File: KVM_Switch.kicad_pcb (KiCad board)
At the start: 2 copper layers, 6 parts, among them J1 HDMI_A, J2 HDMI_A, U1 USB2514B_Bi, U2 STM32C011F4Px, U3 TS3USB221AQRSERQ1, U4 HD3SS215RTQR

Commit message: Moved stuff armound & added components
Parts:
- added J3: USB_C_Receptacle_USB2.0_16P, Connector_USB:USB_C_Receptacle_GCT_USB4105-xx-A_16P_TopMnt_Horizontal, F.Cu at (188.8, 110.6)
- added J4: USB_C_Receptacle_USB2.0_16P, Connector_USB:USB_C_Receptacle_GCT_USB4105-xx-A_16P_TopMnt_Horizontal, F.Cu at (188.8, 120.6)
- added J5: USB_C_Receptacle_USB2.0_16P, Connector_USB:USB_C_Receptacle_GCT_USB4105-xx-A_16P_TopMnt_Horizontal, F.Cu at (188.8, 130.6)
- added U5: TPD12S016PWR, Package_SO:TSSOP-24_4.4x7.8mm_P0.65mm, F.Cu at (113.0, 91.3)
- moved J2 33.9 mm to (158.9, 77.7)
- moved U3 3.86 mm to (153.1, 123.4)
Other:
- board outline added: 100 x 100 mm

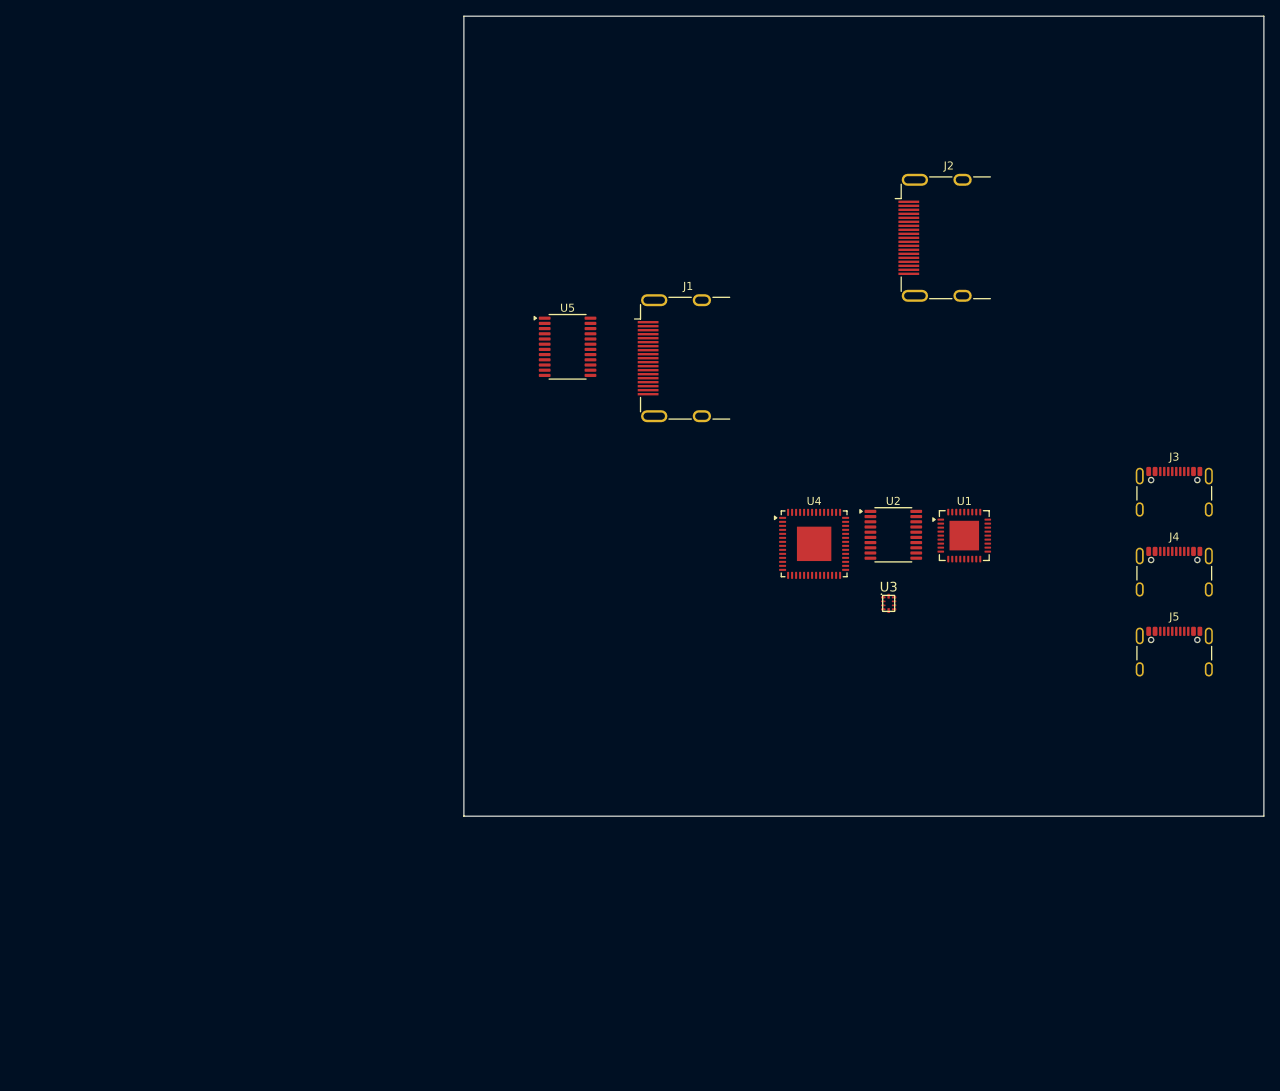
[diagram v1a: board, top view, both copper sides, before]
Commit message: Updated library structure
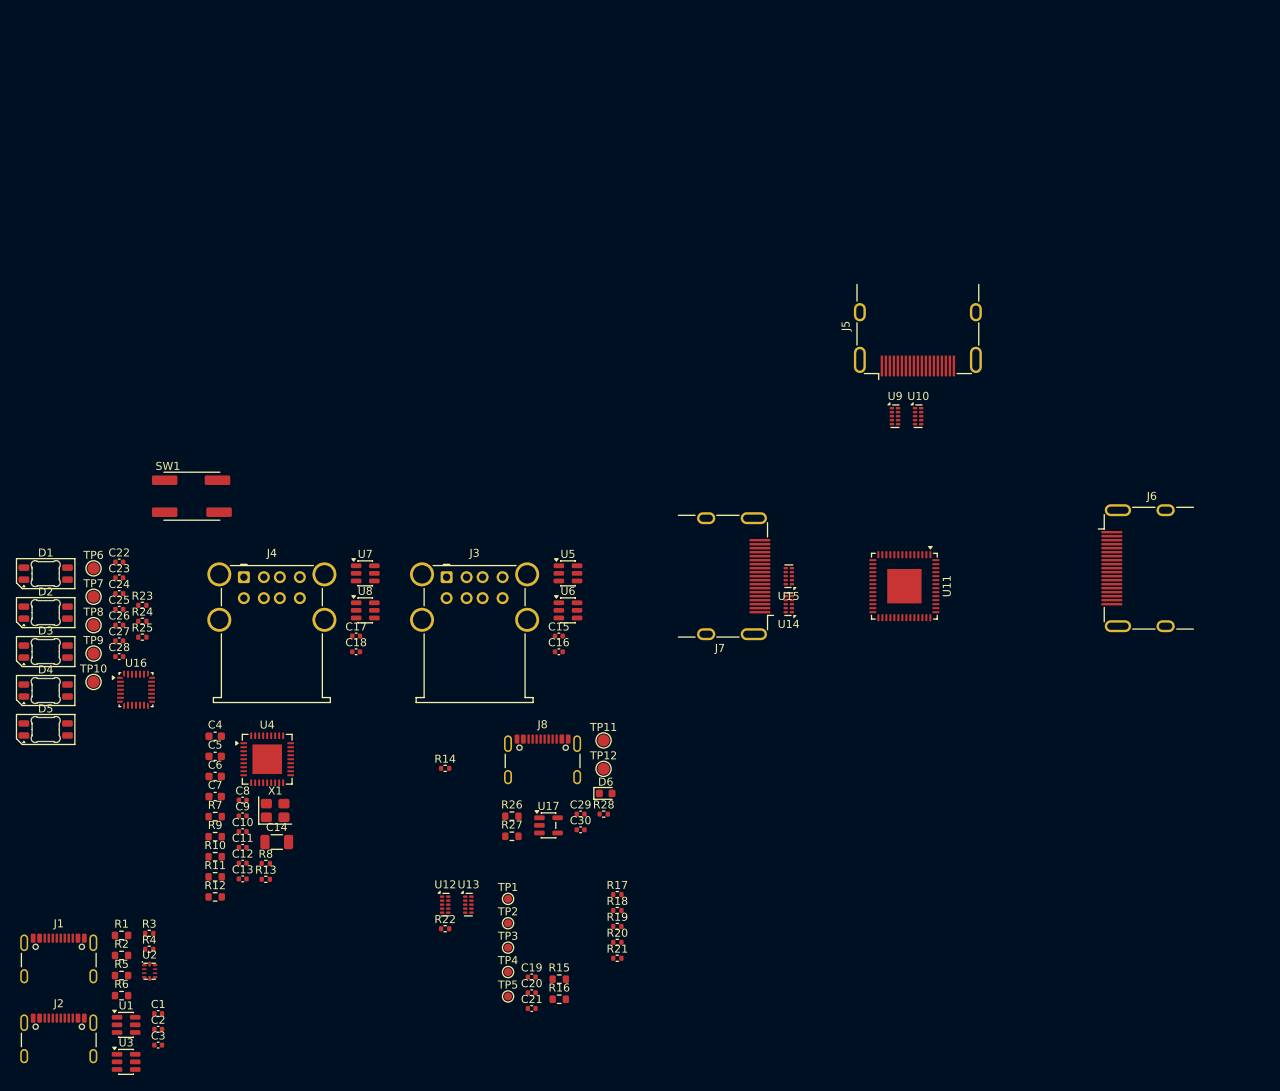
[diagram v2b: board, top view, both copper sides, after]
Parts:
- added C1: 1u, Capacitor_SMD:C_0402_1005Metric, F.Cu at (61.8, 174.7)
- added C10: 1u, Capacitor_SMD:C_0402_1005Metric, F.Cu at (72.3, 151.9)
- added C11: 1u, Capacitor_SMD:C_0402_1005Metric, F.Cu at (72.3, 153.9)
- added C12: 1u, Capacitor_SMD:C_0402_1005Metric, F.Cu at (72.3, 155.9)
- added C13: 1u, Capacitor_SMD:C_0402_1005Metric, F.Cu at (72.3, 157.8)
- added C14: 100u, Capacitor_SMD:C_1206_3216Metric, F.Cu at (76.6, 153.2)
- added C15: 1u, Capacitor_SMD:C_0402_1005Metric, F.Cu at (111.9, 127.5)
- added C16: 1u, Capacitor_SMD:C_0402_1005Metric, F.Cu at (111.9, 129.4)
- added C17: 1u, Capacitor_SMD:C_0402_1005Metric, F.Cu at (86.5, 127.5)
- added C18: 1u, Capacitor_SMD:C_0402_1005Metric, F.Cu at (86.5, 129.4)
- added C19: 1u, Capacitor_SMD:C_0402_1005Metric, F.Cu at (108.5, 170.1)
- added C2: 1u, Capacitor_SMD:C_0402_1005Metric, F.Cu at (61.8, 176.6)
- added C20: 1u, Capacitor_SMD:C_0402_1005Metric, F.Cu at (108.5, 172.1)
- added C21: 1u, Capacitor_SMD:C_0402_1005Metric, F.Cu at (108.5, 174.0)
- added C22: 1u, Capacitor_SMD:C_0402_1005Metric, F.Cu at (56.9, 118.2)
- added C23: 1u, Capacitor_SMD:C_0402_1005Metric, F.Cu at (56.9, 120.2)
- added C24: 1u, Capacitor_SMD:C_0402_1005Metric, F.Cu at (56.9, 122.2)
- added C25: 1u, Capacitor_SMD:C_0402_1005Metric, F.Cu at (56.9, 124.1)
- added C26: 1u, Capacitor_SMD:C_0402_1005Metric, F.Cu at (56.9, 126.1)
- added C27: 1u, Capacitor_SMD:C_0402_1005Metric, F.Cu at (56.9, 128.1)
- added C28: 1u, Capacitor_SMD:C_0402_1005Metric, F.Cu at (56.9, 130.1)
- added C29: 1u, Capacitor_SMD:C_0402_1005Metric, F.Cu at (114.6, 149.7)
- added C3: 1u, Capacitor_SMD:C_0402_1005Metric, F.Cu at (61.8, 178.6)
- added C30: 1u, Capacitor_SMD:C_0402_1005Metric, F.Cu at (114.6, 151.7)
- added C4: 10p, Capacitor_SMD:C_0603_1608Metric, F.Cu at (68.9, 140.0)
- added C5: 100n, Capacitor_SMD:C_0603_1608Metric, F.Cu at (68.9, 142.5)
- added C6: 10p, Capacitor_SMD:C_0603_1608Metric, F.Cu at (68.9, 145.0)
- added C7: 100n, Capacitor_SMD:C_0603_1608Metric, F.Cu at (68.9, 147.5)
- added C8: 1u, Capacitor_SMD:C_0402_1005Metric, F.Cu at (72.3, 148.0)
- added C9: 1u, Capacitor_SMD:C_0402_1005Metric, F.Cu at (72.3, 150.0)
- added D1: SK6812MINI-E, LED_SMD:LED_SK6812MINI-E_3.2x2.8mm_P1.5mm_ReverseMount, F.Cu at (47.7, 119.7)
- added D2: SK6812MINI-E, LED_SMD:LED_SK6812MINI-E_3.2x2.8mm_P1.5mm_ReverseMount, F.Cu at (47.7, 124.5)
- added D3: SK6812MINI-E, LED_SMD:LED_SK6812MINI-E_3.2x2.8mm_P1.5mm_ReverseMount, F.Cu at (47.7, 129.4)
- added D4: SK6812MINI-E, LED_SMD:LED_SK6812MINI-E_3.2x2.8mm_P1.5mm_ReverseMount, F.Cu at (47.7, 134.3)
- added D5: SK6812MINI-E, LED_SMD:LED_SK6812MINI-E_3.2x2.8mm_P1.5mm_ReverseMount, F.Cu at (47.7, 139.2)
- added D6: GLED, LED_SMD:LED_0603_1608Metric, F.Cu at (117.7, 147.2)
- added J6: HDMI_A, Connector_Video:HDMI_A_Molex_208658-1001_Horizontal, F.Cu at (184.3, 119.0)
- added J7: HDMI_A, Connector_Video:HDMI_A_Molex_208658-1001_Horizontal, F.Cu at (133.7, 120.0)
- added J8: USB_C_Receptacle_USB2.0_16P, Connector_USB:USB_C_Receptacle_GCT_USB4105-xx-A_16P_TopMnt_Horizontal, F.Cu at (109.8, 144.0)
- added R1: 5.1k, Resistor_SMD:R_0603_1608Metric, F.Cu at (57.2, 164.9)
- added R10: 100k, Resistor_SMD:R_0603_1608Metric, F.Cu at (68.9, 155.1)
- added R11: 100k, Resistor_SMD:R_0603_1608Metric, F.Cu at (68.9, 157.6)
- added R12: 100k, Resistor_SMD:R_0603_1608Metric, F.Cu at (68.9, 160.1)
- added R13: 10k, Resistor_SMD:R_0402_1005Metric, F.Cu at (75.2, 157.9)
- added R14: 10k, Resistor_SMD:R_0402_1005Metric, F.Cu at (97.7, 144.0)
- added R15: 100k, Resistor_SMD:R_0603_1608Metric, F.Cu at (111.9, 170.4)
- added R16: 100k, Resistor_SMD:R_0603_1608Metric, F.Cu at (111.9, 172.9)
- added R17: 47k, Resistor_SMD:R_0402_1005Metric, F.Cu at (119.2, 159.8)
- added R18: 10k, Resistor_SMD:R_0402_1005Metric, F.Cu at (119.2, 161.8)
- added R19: 47k, Resistor_SMD:R_0402_1005Metric, F.Cu at (119.2, 163.8)
- added R2: 5.1k, Resistor_SMD:R_0603_1608Metric, F.Cu at (57.2, 167.4)
- added R20: 10k, Resistor_SMD:R_0402_1005Metric, F.Cu at (119.2, 165.8)
- added R21: 10k, Resistor_SMD:R_0402_1005Metric, F.Cu at (119.2, 167.8)
- added R22: 10k, Resistor_SMD:R_0402_1005Metric, F.Cu at (97.7, 164.1)
- added R23: 10k, Resistor_SMD:R_0402_1005Metric, F.Cu at (59.8, 123.6)
- added R24: 10k, Resistor_SMD:R_0402_1005Metric, F.Cu at (59.8, 125.6)
- added R25: 10k, Resistor_SMD:R_0402_1005Metric, F.Cu at (59.8, 127.6)
- added R26: 5.1k, Resistor_SMD:R_0603_1608Metric, F.Cu at (106.0, 150.0)
- added R27: 5.1k, Resistor_SMD:R_0603_1608Metric, F.Cu at (106.0, 152.5)
- added R28: 470, Resistor_SMD:R_0402_1005Metric, F.Cu at (117.5, 149.7)
- added R3: 10k, Resistor_SMD:R_0402_1005Metric, F.Cu at (60.7, 164.6)
- added R4: 10k, Resistor_SMD:R_0402_1005Metric, F.Cu at (60.7, 166.6)
- added R5: 5.1k, Resistor_SMD:R_0603_1608Metric, F.Cu at (57.2, 169.9)
- added R6: 5.1k, Resistor_SMD:R_0603_1608Metric, F.Cu at (57.2, 172.4)
- added R7: 100k, Resistor_SMD:R_0603_1608Metric, F.Cu at (68.9, 150.1)
- added R8: 10k, Resistor_SMD:R_0402_1005Metric, F.Cu at (75.2, 155.9)
- added R9: 12k, Resistor_SMD:R_0603_1608Metric, F.Cu at (68.9, 152.6)
- added SW1: SPST-NO, KVM_Swtich:EVQ-Q2K03W, F.Cu at (66.0, 110.0)
- added TP1: TestPoint, TestPoint:TestPoint_Pad_D1.0mm, F.Cu at (105.5, 160.3)
- added TP10: TestPoint, TestPoint:TestPoint_Pad_D1.5mm, F.Cu at (53.7, 133.2)
- added TP11: TestPoint, TestPoint:TestPoint_Pad_D1.5mm, F.Cu at (117.5, 140.5)
- added TP12: TestPoint, TestPoint:TestPoint_Pad_D1.5mm, F.Cu at (117.5, 144.1)
- added TP2: TestPoint, TestPoint:TestPoint_Pad_D1.0mm, F.Cu at (105.5, 163.4)
- added TP3: TestPoint, TestPoint:TestPoint_Pad_D1.0mm, F.Cu at (105.5, 166.4)
- added TP4: TestPoint, TestPoint:TestPoint_Pad_D1.0mm, F.Cu at (105.5, 169.5)
- added TP5: TestPoint, TestPoint:TestPoint_Pad_D1.0mm, F.Cu at (105.5, 172.5)
- added TP6: TestPoint, TestPoint:TestPoint_Pad_D1.5mm, F.Cu at (53.7, 119.0)
- added TP7: TestPoint, TestPoint:TestPoint_Pad_D1.5mm, F.Cu at (53.7, 122.6)
- added TP8: TestPoint, TestPoint:TestPoint_Pad_D1.5mm, F.Cu at (53.7, 126.1)
- added TP9: TestPoint, TestPoint:TestPoint_Pad_D1.5mm, F.Cu at (53.7, 129.7)
- added U10: TPD4E02B04DQA, Package_SON:USON-10_2.5x1.0mm_P0.5mm, F.Cu at (156.8, 100.0)
- added U11: HD3SS215RTQR, Package_DFN_QFN:QFN-56-1EP_8x8mm_P0.5mm_EP4.3x4.3mm, F.Cu at (155.1, 121.2)
- added U12: TPD4E02B04DQA, Package_SON:USON-10_2.5x1.0mm_P0.5mm, F.Cu at (97.7, 161.1)
- added U13: TPD4E02B04DQA, Package_SON:USON-10_2.5x1.0mm_P0.5mm, F.Cu at (100.6, 161.1)
- added U14: TPD4E02B04DQA, Package_SON:USON-10_2.5x1.0mm_P0.5mm, F.Cu at (140.6, 123.5)
- added U15: TPD4E02B04DQA, Package_SON:USON-10_2.5x1.0mm_P0.5mm, F.Cu at (140.6, 120.0)
- added U16: STM32C031G6Ux, Package_DFN_QFN:QFN-28_4x4mm_P0.5mm, F.Cu at (59.0, 134.2)
- added U17: TLV75533PDBV, Package_TO_SOT_SMD:SOT-23-5, F.Cu at (110.6, 151.1)
- added U6: USBLC6-2SC6, Package_TO_SOT_SMD:SOT-23-6, F.Cu at (113.0, 124.3)
- added U7: USBLC6-2SC6, Package_TO_SOT_SMD:SOT-23-6, F.Cu at (87.7, 119.6)
- added U8: USBLC6-2SC6, Package_TO_SOT_SMD:SOT-23-6, F.Cu at (87.7, 124.3)
- added U9: TPD4E02B04DQA, Package_SON:USON-10_2.5x1.0mm_P0.5mm, F.Cu at (153.9, 100.0)
- added X1: 24MHz, Crystal:Crystal_SMD_3225-4Pin_3.2x2.5mm, F.Cu at (76.4, 149.3)
- J1, J2: value HDMI_A -> USB_C_Receptacle_USB2.0_16P; footprint Connector_Video:HDMI_A_Molex_208658-1001_Horizontal -> Connector_USB:USB_C_Receptacle_GCT_USB4105-xx-A_16P_TopMnt_Horizontal
- J3, J4: value USB_C_Receptacle_USB2.0_16P -> USB_A_Stacked; footprint Connector_USB:USB_C_Receptacle_GCT_USB4105-xx-A_16P_TopMnt_Horizontal -> Connector_USB:USB_A_Wuerth_61400826021_Horizontal_Stacked
- J5: value USB_C_Receptacle_USB2.0_16P -> HDMI_A; footprint Connector_USB:USB_C_Receptacle_GCT_USB4105-xx-A_16P_TopMnt_Horizontal -> Connector_Video:HDMI_A_Molex_208658-1001_Horizontal
- U1: value USB2514B_Bi -> USBLC6-2SC6; footprint Package_DFN_QFN:QFN-36-1EP_6x6mm_P0.5mm_EP3.7x3.7mm -> Package_TO_SOT_SMD:SOT-23-6
- U2: value STM32C011F4Px -> TS3USB221AQRSERQ1; footprint Package_SO:TSSOP-20_4.4x6.5mm_P0.65mm -> TS3USB221AQRSERQ1:TS3USB221AQRSERQ1
- U3: value TS3USB221AQRSERQ1 -> USBLC6-2SC6; footprint TS3USB221AQRSERQ1:TS3USB221AQRSERQ1 -> Package_TO_SOT_SMD:SOT-23-6
- U4: value HD3SS215RTQR -> USB2514B_Bi; footprint Package_DFN_QFN:QFN-56-1EP_8x8mm_P0.5mm_EP4.3x4.3mm -> Package_DFN_QFN:QFN-36-1EP_6x6mm_P0.5mm_EP3.7x3.7mm
- U5: value TPD12S016PWR -> USBLC6-2SC6; footprint Package_SO:TSSOP-24_4.4x7.8mm_P0.65mm -> Package_TO_SOT_SMD:SOT-23-6
- moved J2 149.1 mm to (49.4, 178.9)
- moved U1 121.3 mm to (57.8, 176.1)
- moved J4 116.3 mm to (72.5, 120.1)
- moved U3 111.2 mm to (57.8, 180.7)
- moved J1 108.3 mm to (49.4, 168.9)
- moved U2 107.8 mm to (60.7, 169.4)
- moved J3 91.5 mm to (97.8, 120.1)
- moved U4 73.5 mm to (75.4, 142.9)
- moved J5 51.4 mm to (156.8, 90.4), turned to 90 degrees
- moved U5 28.3 mm to (113.0, 119.6)
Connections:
- J1 pad SH: unconnected-(J1-PadSH) -> GND
- J2 pad SH: unconnected-(J2-PadSH) -> GND
- J3 pad SH: unconnected-(J3-SHIELD-PadSH) -> Net-(J3-GND2)
- J4 pad SH: unconnected-(J4-SHIELD-PadSH) -> Net-(J4-GND2)
- J5 pad SH: unconnected-(J5-SHIELD-PadSH) -> GND
- U1 pad 1: unconnected-(U1-USBDM_DN1/PRT_DIS_M1-Pad1) -> /USB_Host_Select/USB_CONN_A_DN
- U1 pad 2: unconnected-(U1-USBDP_DN1/PRT_DIS_P1-Pad2) -> GND
- U1 pad 3: unconnected-(U1-USBDM_DN2/PRT_DIS_M2-Pad3) -> /USB_Host_Select/USB_CONN_A_DP
- U1 pad 4: unconnected-(U1-USBDP_DN2/PRT_DIS_P2-Pad4) -> /USB_Host_Select/USB_A_DP
- U1 pad 5: unconnected-(U1-VDDA33-Pad5) -> Net-(U1-VBUS)
- U1 pad 6: unconnected-(U1-USBDM_DN3/PRT_DIS_M3-Pad6) -> /USB_Host_Select/USB_A_DN
- U2 pad 1: unconnected-(U2-PB7-Pad1) -> /USB_Host_Select/USB_A_DP
- U2 pad 10: unconnected-(U2-PA3-Pad10) -> +3V3
- U2 pad 2: unconnected-(U2-PC14-Pad2) -> /USB_Host_Select/USB_A_DN
- U2 pad 3: unconnected-(U2-PC15-Pad3) -> /USB_Host_Select/USB_B_DP
- U2 pad 4: unconnected-(U2-VDD-Pad4) -> /USB_Host_Select/USB_B_DN
- U2 pad 5: unconnected-(U2-VSS-Pad5) -> GND
- U2 pad 6: unconnected-(U2-PF2-Pad6) -> Net-(U2-~{OE})
- U2 pad 7: unconnected-(U2-PA0-Pad7) -> /UBS_Hub/USB_UP_DN
- U2 pad 8: unconnected-(U2-PA1-Pad8) -> /UBS_Hub/USB_UP_DP
- U2 pad 9: unconnected-(U2-PA2-Pad9) -> /SW
- U3 pad 1: unconnected-(U3-1D+-Pad1) -> /USB_Host_Select/USB_CONN_B_DN
- U3 pad 2: unconnected-(U3-1D--Pad2) -> GND
- U3 pad 3: unconnected-(U3-2D+-Pad3) -> /USB_Host_Select/USB_CONN_B_DP
- U3 pad 4: unconnected-(U3-2D--Pad4) -> /USB_Host_Select/USB_B_DP
- U3 pad 5: unconnected-(U3-GND-Pad5) -> Net-(U3-VBUS)
- U3 pad 6: unconnected-(U3-OE-Pad6) -> /USB_Host_Select/USB_B_DN
- U4 pad 1: unconnected-(U4-AUX_SEL-Pad1) -> /UBS_Hub/USB_DOWN_1/USB1_DP
- U4 pad 10: GND -> +3V3
- U4 pad 14: unconnected-(U4-AUXC_N-Pad14) -> Net-(U4-CRFILT)
- U4 pad 15: unconnected-(U4-HPDC-Pad15) -> +3V3
- U4 pad 2: unconnected-(U4-DC0_P-Pad2) -> /UBS_Hub/USB_DOWN_1/USB1_DN
- U4 pad 22: unconnected-(U4-DDCCLK_B-Pad22) -> /UBS_Hub/NREM1
- U4 pad 23: unconnected-(U4-DDCDAT_B-Pad23) -> +3V3
- U4 pad 24: unconnected-(U4-AUXB_P-Pad24) -> /UBS_Hub/CFGS0
- U4 pad 25: unconnected-(U4-AUXB_N-Pad25) -> /UBS_Hub/CFGS1
- U4 pad 26: unconnected-(U4-DDCDAT_C-Pad26) -> Net-(U4-RESET_N)
- U4 pad 27: unconnected-(U4-DDCCLK_A-Pad27) -> /MCU/UP_DET
- U4 pad 28: unconnected-(U4-DDCDAT_A-Pad28) -> /UBS_Hub/NREM0
- U4 pad 29: unconnected-(U4-AUXA_N-Pad29) -> +3V3
- U4 pad 3: unconnected-(U4-DC0_N-Pad3) -> /UBS_Hub/USB_DOWN_1/USB2_DN
- U4 pad 30: unconnected-(U4-AUXA_P-Pad30) -> /UBS_Hub/USB_UP_DN
- U4 pad 31: unconnected-(U4-DB3_N-Pad31) -> /UBS_Hub/USB_UP_DP
- U4 pad 32: unconnected-(U4-DB3_P-Pad32) -> /UBS_Hub/HUB_OSCLO
- U4 pad 33: GND -> /UBS_Hub/HUB_OSCIN
- U4 pad 34: unconnected-(U4-DB2_N-Pad34) -> Net-(U4-PLLFILT)
- U4 pad 35: unconnected-(U4-DB2_P-Pad35) -> Net-(U4-RBIAS)
- U4 pad 36: GND -> +3V3
- U4 pad 37: unconnected-(U4-DB1_N-Pad37) -> GND
- U4 pad 4: unconnected-(U4-GND-Pad4) -> /UBS_Hub/USB_DOWN_1/USB2_DP
- U4 pad 5: unconnected-(U4-DC1_P-Pad5) -> +3V3
- U4 pad 6: unconnected-(U4-DC1_N-Pad6) -> /UBS_Hub/USB_DOWN_2/USB1_DP
- U4 pad 7: GND -> /UBS_Hub/USB_DOWN_2/USB1_DN
- U4 pad 8: unconnected-(U4-DC2_P-Pad8) -> /UBS_Hub/USB_DOWN_2/USB2_DN
- U4 pad 9: unconnected-(U4-DC2_N-Pad9) -> /UBS_Hub/USB_DOWN_2/USB2_DP
- U5 pad 1: unconnected-(U5-CEC_A-Pad1) -> /UBS_Hub/USB_DOWN_1/USB1_DP
- U5 pad 2: unconnected-(U5-SCL_A-Pad2) -> GND
- U5 pad 3: unconnected-(U5-SDA_A-Pad3) -> /UBS_Hub/USB_DOWN_1/USB1_DN
- U5 pad 4: unconnected-(U5-HPD_A-Pad4) -> /UBS_Hub/USB_DOWN_1/USB1_CONN_DN
- U5 pad 5: unconnected-(U5-LS_OE-Pad5) -> VBUS
- U5 pad 6: unconnected-(U5-GND_6-Pad6) -> /UBS_Hub/USB_DOWN_1/USB1_CONN_DP
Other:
- board size 100 x 100 mm -> 3.6 x 3.2 mm
- copper layers 2 -> 4

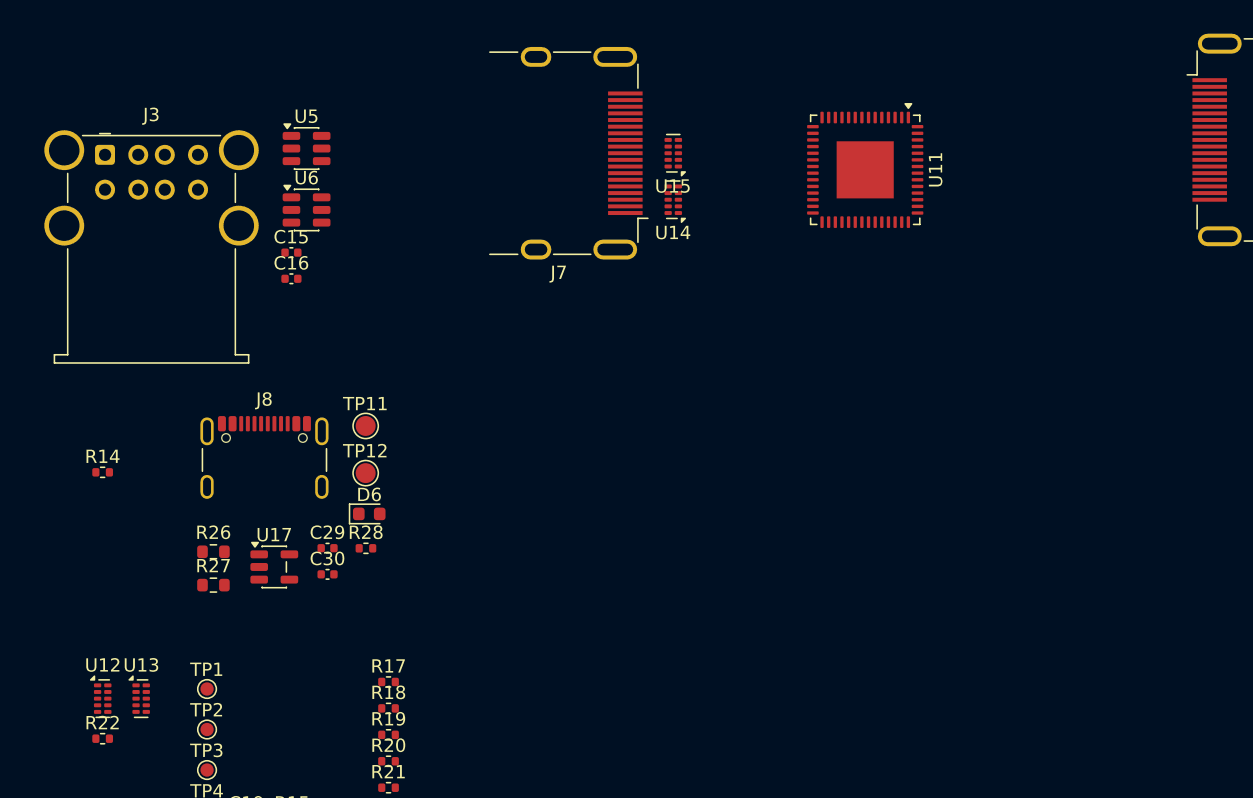
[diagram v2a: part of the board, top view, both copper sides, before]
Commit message: Library and Schematics Fixes
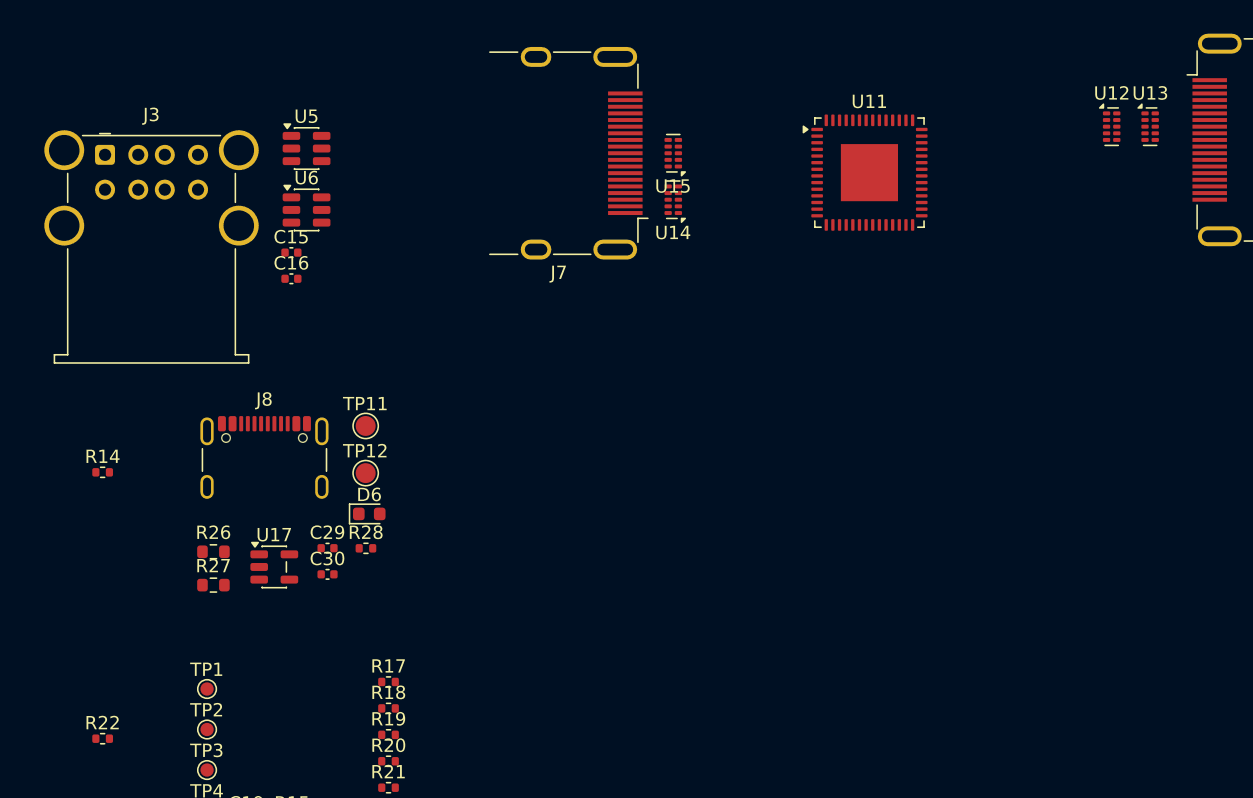
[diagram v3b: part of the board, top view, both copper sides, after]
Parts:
- U2: footprint TS3USB221AQRSERQ1:TS3USB221AQRSERQ1 -> KVM_Swtich:TS3USB221AQRSERQ1
- moved U12 87.3 mm to (173.6, 118.0)
- moved U13 87.3 mm to (176.5, 118.0)
- moved U11 0.38 mm to (155.4, 121.5), turned to 0 degrees

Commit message: More schematics fixes & Layout attempt
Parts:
- added ?: MountingHole_3.2mm_M3_Pad_Via, MountingHole:MountingHole_3.2mm_M3_Pad_Via, F.Cu at (105.0, 70.0)
- added ?: MountingHole_3.2mm_M3_Pad_Via, MountingHole:MountingHole_3.2mm_M3_Pad_Via, F.Cu at (195.0, 70.0)
- added ?: MountingHole_3.2mm_M3_Pad_Via, MountingHole:MountingHole_3.2mm_M3_Pad_Via, F.Cu at (195.0, 130.0)
- added ?: MountingHole_3.2mm_M3_Pad_Via, MountingHole:MountingHole_3.2mm_M3_Pad_Via, F.Cu at (105.0, 130.0)
- added C31: 1u, Capacitor_SMD:C_0402_1005Metric, F.Cu at (170.2, 118.5)
- added TP13: TestPoint, TestPoint:TestPoint_Pad_D1.5mm, F.Cu at (139.2, 123.0)
- added TP14: TestPoint, TestPoint:TestPoint_Pad_D1.5mm, F.Cu at (128.6, 126.0)
- C10, C11, C12, C8, C9, D2, D3, D4, D5: moved to B.Cu
- C14: value 100u -> 1u; footprint Capacitor_SMD:C_1206_3216Metric -> Capacitor_SMD:C_0402_1005Metric
- C19, C20: value 1u -> 10p
- C25: value 1u -> 100u; footprint Capacitor_SMD:C_0402_1005Metric -> Capacitor_SMD:C_1206_3216Metric
- C26, C27: value 1u -> 100n
- C4, C6: value 10p -> 1u; footprint Capacitor_SMD:C_0603_1608Metric -> Capacitor_SMD:C_0402_1005Metric
- C5, C7: value 100n -> 1u; footprint Capacitor_SMD:C_0603_1608Metric -> Capacitor_SMD:C_0402_1005Metric
- D1: value SK6812MINI-E -> GLED; footprint LED_SMD:LED_SK6812MINI-E_3.2x2.8mm_P1.5mm_ReverseMount -> LED_SMD:LED_0603_1608Metric
- D6: value GLED -> SK6812MINI-E; footprint LED_SMD:LED_0603_1608Metric -> LED_SMD:LED_SK6812MINI-E_3.2x2.8mm_P1.5mm_ReverseMount; moved to B.Cu
- J1, J2: value USB_C_Receptacle_USB2.0_16P -> HDMI_A; footprint Connector_USB:USB_C_Receptacle_GCT_USB4105-xx-A_16P_TopMnt_Horizontal -> Connector_Video:HDMI_A_Molex_208658-1001_Horizontal
- J3: value USB_A_Stacked -> HDMI_A; footprint Connector_USB:USB_A_Wuerth_61400826021_Horizontal_Stacked -> Connector_Video:HDMI_A_Molex_208658-1001_Horizontal; moved to B.Cu
- J4: value USB_A_Stacked -> USB_C_Receptacle_USB2.0_16P; footprint Connector_USB:USB_A_Wuerth_61400826021_Horizontal_Stacked -> Connector_USB:USB_C_Receptacle_GCT_USB4105-xx-A_16P_TopMnt_Horizontal
- J5, J6: value HDMI_A -> USB_C_Receptacle_USB2.0_16P; footprint Connector_Video:HDMI_A_Molex_208658-1001_Horizontal -> Connector_USB:USB_C_Receptacle_GCT_USB4105-xx-A_16P_TopMnt_Horizontal
- J7: value HDMI_A -> USB_A_Stacked; footprint Connector_Video:HDMI_A_Molex_208658-1001_Horizontal -> Connector_USB:USB_A_Wuerth_61400826021_Horizontal_Stacked
- J8: value USB_C_Receptacle_USB2.0_16P -> USB_A_Stacked; footprint Connector_USB:USB_C_Receptacle_GCT_USB4105-xx-A_16P_TopMnt_Horizontal -> Connector_USB:USB_A_Wuerth_61400826021_Horizontal_Stacked
- R1, R2, R6: value 5.1k -> 10k; footprint Resistor_SMD:R_0603_1608Metric -> Resistor_SMD:R_0402_1005Metric
- R10, R12, R16: value 100k -> 5.1k
- R11: value 100k -> 470; footprint Resistor_SMD:R_0603_1608Metric -> Resistor_SMD:R_0402_1005Metric
- R15, R7: value 100k -> 10k; footprint Resistor_SMD:R_0603_1608Metric -> Resistor_SMD:R_0402_1005Metric
- R17: value 47k -> 5.1k; footprint Resistor_SMD:R_0402_1005Metric -> Resistor_SMD:R_0603_1608Metric
- R19: value 47k -> 10k
- R20, R21: value 10k -> 5.1k; footprint Resistor_SMD:R_0402_1005Metric -> Resistor_SMD:R_0603_1608Metric
- R24: value 10k -> 12k; footprint Resistor_SMD:R_0402_1005Metric -> Resistor_SMD:R_0603_1608Metric
- R25: value 10k -> 100k
- R26, R27, R5: value 5.1k -> 100k; footprint Resistor_SMD:R_0603_1608Metric -> Resistor_SMD:R_0402_1005Metric
- R28: value 470 -> 100k
- R3, R4: value 10k -> 47k
- R9: value 12k -> 100k; footprint Resistor_SMD:R_0603_1608Metric -> Resistor_SMD:R_0402_1005Metric
- U1, U3, U6, U7: value USBLC6-2SC6 -> TPD4E02B04DQA; footprint Package_TO_SOT_SMD:SOT-23-6 -> Package_SON:USON-10_2.5x1.0mm_P0.5mm
- U10, U12, U14, U15: value TPD4E02B04DQA -> USBLC6-2SC6; footprint Package_SON:USON-10_2.5x1.0mm_P0.5mm -> Package_TO_SOT_SMD:SOT-23-6
- U11: value HD3SS215RTQR -> TS3USB221AQRSERQ1; footprint Package_DFN_QFN:QFN-56-1EP_8x8mm_P0.5mm_EP4.3x4.3mm -> KVM_Swtich:TS3USB221AQRSERQ1
- U13: value TPD4E02B04DQA -> USB2514B_Bi; footprint Package_SON:USON-10_2.5x1.0mm_P0.5mm -> Package_DFN_QFN:QFN-36-1EP_6x6mm_P0.5mm_EP3.7x3.7mm
- U16: value STM32C031G6Ux -> USBLC6-2SC6; footprint Package_DFN_QFN:QFN-28_4x4mm_P0.5mm -> Package_TO_SOT_SMD:SOT-23-6
- U17: value TLV75533PDBV -> USBLC6-2SC6; footprint Package_TO_SOT_SMD:SOT-23-5 -> Package_TO_SOT_SMD:SOT-23-6
- U2: value TS3USB221AQRSERQ1 -> TPD4E02B04DQA; footprint KVM_Swtich:TS3USB221AQRSERQ1 -> Package_SON:USON-10_2.5x1.0mm_P0.5mm
- U4: value USB2514B_Bi -> TPD4E02B04DQA; footprint Package_DFN_QFN:QFN-36-1EP_6x6mm_P0.5mm_EP3.7x3.7mm -> Package_SON:USON-10_2.5x1.0mm_P0.5mm
- U5: value USBLC6-2SC6 -> HD3SS215RTQR; footprint Package_TO_SOT_SMD:SOT-23-6 -> Package_DFN_QFN:QFN-56-1EP_8x8mm_P0.5mm_EP4.3x4.3mm
- U8: value USBLC6-2SC6 -> TLV75533PDBV; footprint Package_TO_SOT_SMD:SOT-23-6 -> Package_TO_SOT_SMD:SOT-23-5
- U9: value TPD4E02B04DQA -> STM32C031G6Ux; footprint Package_SON:USON-10_2.5x1.0mm_P0.5mm -> Package_DFN_QFN:QFN-28_4x4mm_P0.5mm
- moved D2 147.5 mm to (192.0, 94.0), turned to 180 degrees
- moved D3 147.2 mm to (192.0, 100.0), turned to 180 degrees
- moved D4 147.0 mm to (192.0, 106.0), turned to 180 degrees
- moved D5 146.8 mm to (192.0, 112.0), turned to 180 degrees
- moved J2 143.5 mm to (144.0, 71.0), turned to 90 degrees
- moved C13 137.9 mm to (183.0, 75.5), turned to 90 degrees
- moved C8 132.5 mm to (192.0, 91.0)
- moved U3 132.3 mm to (140.8, 77.6), turned to 90 degrees
- moved C9 130.8 mm to (192.0, 97.0)
- moved C7 130.7 mm to (185.0, 87.5), turned to -90 degrees
- moved C10 129.3 mm to (192.0, 102.9)
- moved SW1 128.3 mm to (192.0, 86.0)
- moved C11 127.8 mm to (192.0, 109.0)
- moved R2 127.4 mm to (148.0, 78.0), turned to -90 degrees
- moved C12 126.4 mm to (192.0, 115.0)
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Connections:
- C1 pad 1: Net-(U1-VBUS) -> +3V3
- C10 pad 1: +3V3 -> VBUS
- C11 pad 1: +3V3 -> VBUS
- C12 pad 1: +3V3 -> VBUS
- C13 pad 1: +3V3 -> /MCU/DET_USB_A
- C14 pad 1: VBUS -> +3V3
- C15 pad 1: GND -> /MCU/DET_USB_B
- C15 pad 2: VBUS -> GND
- C16 pad 1: GND -> +3V3
- C16 pad 2: VBUS -> GND
- C17 pad 1: GND -> +3V3
- C17 pad 2: VBUS -> GND
- C18 pad 1: GND -> +3V3
- C18 pad 2: VBUS -> GND
- C19 pad 1: +3V3 -> /USB_Hub/HUB_OSCIN
- C20 pad 1: +3V3 -> /USB_Hub/HUB_OSCLO
- C21 pad 1: VBUS -> +3V3
- C24 pad 1: /MCU/BNT -> Net-(U13-RESET_N)
- C25 pad 1: +3V3 -> VBUS
- C26 pad 1: +3V3 -> GND
- C26 pad 2: GND -> Net-(U13-PLLFILT)
- C27 pad 1: +3V3 -> GND
- C27 pad 2: GND -> Net-(U13-CRFILT)
- C28 pad 1: +3V3 -> GND
- C28 pad 2: GND -> VBUS
- C29 pad 1: VBUS -> GND
- C29 pad 2: GND -> VBUS
- C3 pad 1: Net-(U3-VBUS) -> VBUS
- C30 pad 1: +3V3 -> GND
- C30 pad 2: GND -> VBUS
- C4 pad 1: /UBS_Hub/HUB_OSCIN -> VBUS
- C5 pad 1: GND -> +3V3
- C5 pad 2: Net-(U4-PLLFILT) -> GND
- C6 pad 1: /UBS_Hub/HUB_OSCLO -> +3V3
- C7 pad 1: GND -> /MCU/BTN
- C7 pad 2: Net-(U4-CRFILT) -> GND
- C8 pad 1: +3V3 -> VBUS
- C9 pad 1: +3V3 -> VBUS
- D1 pad 1: GND -> Net-(D1-K)
- D1 pad 2: /MCU/LED -> +3V3
- D2 pad 2: Net-(D1-DOUT) -> /MCU/LED
- D2 pad 3: +3V3 -> VBUS
- D3 pad 3: +3V3 -> VBUS
- D4 pad 3: +3V3 -> VBUS
- D5 pad 3: +3V3 -> VBUS
- D5 pad 4: unconnected-(D5-DOUT-Pad4) -> Net-(D5-DOUT)
- D6 pad 1: Net-(D6-K) -> GND
- D6 pad 2: +3V3 -> Net-(D5-DOUT)
- J3 pad 1: VBUS -> /HDMI_Switch/HDMI_OUT/D2_P
- J3 pad 2: /UBS_Hub/USB_DOWN_1/USB1_CONN_DN -> GND
- J3 pad 3: /UBS_Hub/USB_DOWN_1/USB1_CONN_DP -> /HDMI_Switch/HDMI_OUT/D2_N
- J3 pad 4: GND -> /HDMI_Switch/HDMI_OUT/D1_P
- J3 pad 5: VBUS -> GND
- J3 pad 6: /UBS_Hub/USB_DOWN_1/USB2_CONN_DN -> /HDMI_Switch/HDMI_OUT/D1_N
- J3 pad 7: /UBS_Hub/USB_DOWN_1/USB2_CONN_DP -> /HDMI_Switch/HDMI_OUT/D0_P
- J3 pad 8: Net-(J3-GND2) -> GND
- J3 pad SH: Net-(J3-GND2) -> GND
- J4 pad SH: Net-(J4-GND2) -> GND
- J7 pad 1: /HDMI_Switch/HDMI_OUT/D2_P -> VBUS
- J7 pad 2: GND -> /USB_Hub/USB_DOWN_1/USB1_CONN_DN
- J7 pad 3: /HDMI_Switch/HDMI_OUT/D2_N -> /USB_Hub/USB_DOWN_1/USB1_CONN_DP
- J7 pad 4: /HDMI_Switch/HDMI_OUT/D1_P -> GND
- J7 pad 5: GND -> VBUS
- J7 pad 6: /HDMI_Switch/HDMI_OUT/D1_N -> /USB_Hub/USB_DOWN_1/USB2_CONN_DN
- J7 pad 7: /HDMI_Switch/HDMI_OUT/D0_P -> /USB_Hub/USB_DOWN_1/USB2_CONN_DP
- J7 pad 8: GND -> Net-(J7-GND2)
- J7 pad SH: GND -> Net-(J7-GND2)
- J8 pad SH: GND -> Net-(J8-GND2)
- R1 pad 1: GND -> Net-(J1-+5V)
- R1 pad 2: Net-(J1-CC1) -> /HDMI_Switch/DET_A
- R10 pad 2: /UBS_Hub/NREM1 -> Net-(J4-CC1)
- R11 pad 1: GND -> Net-(D1-K)
- R11 pad 2: /UBS_Hub/NREM0 -> GND
- R12 pad 2: /UBS_Hub/CFGS1 -> Net-(J4-CC2)
- R13 pad 2: /MCU/UP_DET -> /MCU/RST
- R14 pad 1: Net-(J5-+5V) -> +3V3
- R14 pad 2: /HDMI_Switch/DET_A -> Net-(R14-Pad2)
- R15 pad 1: GND -> Net-(R14-Pad2)
- R15 pad 2: /HDMI_Switch/HDMI_IN_A/HPD -> /MCU/BTN
- R16 pad 2: /HDMI_Switch/HDMI_IN_B/HPD -> Net-(J5-CC1)
- R17 pad 1: /HDMI_Switch/HDMI_OUT/SCL -> GND
- R17 pad 2: VBUS -> Net-(J5-CC2)
- R18 pad 1: /SW -> /MCU/USB_SW
- R19 pad 1: /HDMI_Switch/HDMI_OUT/SDA -> Net-(U11-~{OE})
- R19 pad 2: VBUS -> GND
- R2 pad 1: GND -> Net-(J2-+5V)
- R2 pad 2: Net-(J1-CC2) -> /HDMI_Switch/DET_B
- R20 pad 1: +3V3 -> GND
- R20 pad 2: Net-(U11-AUX_SEL) -> Net-(J6-CC1)
- R21 pad 1: Net-(U11-AUX_SEL) -> GND
- R21 pad 2: GND -> Net-(J6-CC2)
- R22 pad 1: Net-(J6-+5V) -> +3V3
- R22 pad 2: /HDMI_Switch/DET_B -> /MCU/UP_DET
- R23 pad 2: /MCU/RST -> Net-(U13-RESET_N)
- R24 pad 1: +3V3 -> GND
- R24 pad 2: Net-(R24-Pad2) -> Net-(U13-RBIAS)
- R25 pad 1: Net-(R24-Pad2) -> GND
- R25 pad 2: /MCU/BNT -> /USB_Hub/CFGS0
- R26 pad 2: Net-(J8-CC1) -> /USB_Hub/NREM1
- R27 pad 2: Net-(J8-CC2) -> /USB_Hub/NREM0
- R28 pad 1: Net-(D6-K) -> GND
- R28 pad 2: GND -> /USB_Hub/CFGS1
- R3 pad 1: Net-(U2-~{OE}) -> /HDMI_Switch/HDMI_OUT/SCL
- R3 pad 2: GND -> VBUS
- R4 pad 1: /SW -> /HDMI_Switch/HDMI_OUT/SDA
- R4 pad 2: GND -> VBUS
- R5 pad 2: Net-(J2-CC1) -> /HDMI_Switch/HDMI_IN_A/HPD
- R6 pad 1: GND -> +3V3
- R6 pad 2: Net-(J2-CC2) -> Net-(U5-AUX_SEL)
- R7 pad 1: GND -> Net-(U5-AUX_SEL)
- R7 pad 2: /UBS_Hub/CFGS0 -> GND
- R8 pad 1: +3V3 -> /HDMI_Switch/SW
- R8 pad 2: Net-(U4-RESET_N) -> GND
- R9 pad 2: Net-(U4-RBIAS) -> /HDMI_Switch/HDMI_IN_B/HPD
- SW1 pad 1: Net-(R24-Pad2) -> Net-(R14-Pad2)
- SW1 pad 2: Net-(R24-Pad2) -> Net-(R14-Pad2)
- TP10 pad 1: /MCU/SWCLK -> /MCU/UART_TX
- TP11 pad 1: VBUS -> /MCU/UART_RX
- TP12 pad 1: +3V3 -> /MCU/SWDIO
- TP2 pad 1: /HDMI_Switch/DET_B -> /HDMI_Switch/HDMI_IN_A/CEC
- TP3 pad 1: /HDMI_Switch/HDMI_IN_A/CEC -> /HDMI_Switch/HDMI_OUT/CEC
- TP4 pad 1: /HDMI_Switch/HDMI_IN_B/CEC -> /HDMI_Switch/DET_B
- TP5 pad 1: /HDMI_Switch/HDMI_OUT/CEC -> /HDMI_Switch/HDMI_IN_B/CEC
- TP6 pad 1: /MCU/RST -> VBUS
- TP7 pad 1: /MCU/UART_TX -> +3V3
- TP8 pad 1: /MCU/UART_RX -> +3V3
- TP9 pad 1: /MCU/SWDIO -> /MCU/RST
- U1 pad 1: /USB_Host_Select/USB_CONN_A_DN -> /HDMI_Switch/HDMI_IN_A/D2_P
- U1 pad 2: GND -> /HDMI_Switch/HDMI_IN_A/D2_N
- U1 pad 3: /USB_Host_Select/USB_CONN_A_DP -> GND
- U1 pad 4: /USB_Host_Select/USB_A_DP -> /HDMI_Switch/HDMI_IN_A/D1_P
- U1 pad 5: Net-(U1-VBUS) -> /HDMI_Switch/HDMI_IN_A/D1_N
- U1 pad 6: /USB_Host_Select/USB_A_DN -> /HDMI_Switch/HDMI_IN_A/D1_N
- U10 pad 1: /HDMI_Switch/HDMI_IN_A/D0_P -> /USB_Host_Select/USB_CONN_A_DN
- U10 pad 2: /HDMI_Switch/HDMI_IN_A/D0_N -> GND
- U10 pad 3: GND -> /USB_Host_Select/USB_CONN_A_DP
- U10 pad 4: /HDMI_Switch/HDMI_IN_A/CK_P -> /USB_Host_Select/USB_A_DP
- U10 pad 5: /HDMI_Switch/HDMI_IN_A/CK_N -> /MCU/DET_USB_A
- U10 pad 6: /HDMI_Switch/HDMI_IN_A/CK_N -> /USB_Host_Select/USB_A_DN
- U11 pad 1: Net-(U11-AUX_SEL) -> /USB_Host_Select/USB_A_DN
- U11 pad 10: GND -> +3V3
- U11 pad 2: /HDMI_Switch/HDMI_OUT/D0_P -> /USB_Host_Select/USB_A_DP
- U11 pad 3: /HDMI_Switch/HDMI_OUT/D0_N -> /USB_Host_Select/USB_B_DN
- U11 pad 4: GND -> /USB_Host_Select/USB_B_DP
- U11 pad 5: /HDMI_Switch/HDMI_OUT/D1_P -> GND
- U11 pad 6: /HDMI_Switch/HDMI_OUT/D1_N -> Net-(U11-~{OE})
- U11 pad 7: GND -> /USB_Host_Select/USB_UP_DP
- U11 pad 8: /HDMI_Switch/HDMI_OUT/D2_P -> /USB_Host_Select/USB_UP_DN
- U11 pad 9: /HDMI_Switch/HDMI_OUT/D2_N -> /MCU/USB_SW
- U12 pad 1: /HDMI_Switch/HDMI_IN_B/D2_P -> /USB_Host_Select/USB_CONN_B_DN
- U12 pad 2: /HDMI_Switch/HDMI_IN_B/D2_N -> GND
- U12 pad 3: GND -> /USB_Host_Select/USB_CONN_B_DP
- U12 pad 4: /HDMI_Switch/HDMI_IN_B/D1_P -> /USB_Host_Select/USB_B_DP
- U12 pad 5: /HDMI_Switch/HDMI_IN_B/D1_N -> /MCU/DET_USB_B
- U12 pad 6: /HDMI_Switch/HDMI_IN_B/D1_N -> /USB_Host_Select/USB_B_DN
- U13 pad 1: /HDMI_Switch/HDMI_IN_B/D0_P -> /USB_Hub/USB_DOWN_1/USB1_DN
- U13 pad 10: /HDMI_Switch/HDMI_IN_B/D0_P -> +3V3
- U13 pad 2: /HDMI_Switch/HDMI_IN_B/D0_N -> /USB_Hub/USB_DOWN_1/USB1_DP
- U13 pad 3: GND -> /USB_Hub/USB_DOWN_1/USB2_DN
- U13 pad 4: /HDMI_Switch/HDMI_IN_B/CK_P -> /USB_Hub/USB_DOWN_1/USB2_DP
- U13 pad 5: /HDMI_Switch/HDMI_IN_B/CK_N -> +3V3
- U13 pad 6: /HDMI_Switch/HDMI_IN_B/CK_N -> /USB_Hub/USB_DOWN_2/USB1_DN
- U13 pad 7: /HDMI_Switch/HDMI_IN_B/CK_P -> /USB_Hub/USB_DOWN_2/USB1_DP
- U13 pad 8: GND -> /USB_Hub/USB_DOWN_2/USB2_DN
- U13 pad 9: /HDMI_Switch/HDMI_IN_B/D0_N -> /USB_Hub/USB_DOWN_2/USB2_DP
- U14 pad 1: /HDMI_Switch/HDMI_OUT/D2_P -> /USB_Hub/USB_DOWN_1/USB1_DP
- U14 pad 2: /HDMI_Switch/HDMI_OUT/D2_N -> GND
- U14 pad 3: GND -> /USB_Hub/USB_DOWN_1/USB1_DN
- U14 pad 4: /HDMI_Switch/HDMI_OUT/D1_P -> /USB_Hub/USB_DOWN_1/USB1_CONN_DN
- U14 pad 5: /HDMI_Switch/HDMI_OUT/D1_N -> VBUS
- U14 pad 6: /HDMI_Switch/HDMI_OUT/D1_N -> /USB_Hub/USB_DOWN_1/USB1_CONN_DP
- U15 pad 1: /HDMI_Switch/HDMI_OUT/D0_P -> /USB_Hub/USB_DOWN_1/USB2_DP
- U15 pad 2: /HDMI_Switch/HDMI_OUT/D0_N -> GND
- U15 pad 3: GND -> /USB_Hub/USB_DOWN_1/USB2_DN
- U15 pad 4: /HDMI_Switch/HDMI_OUT/CK_P -> /USB_Hub/USB_DOWN_1/USB2_CONN_DN
- U15 pad 5: /HDMI_Switch/HDMI_OUT/CK_N -> VBUS
- U15 pad 6: /HDMI_Switch/HDMI_OUT/CK_N -> /USB_Hub/USB_DOWN_1/USB2_CONN_DP
- U16 pad 1: unconnected-(U16-PC14-Pad1) -> /USB_Hub/USB_DOWN_2/USB1_DP
- U16 pad 2: unconnected-(U16-PC15-Pad2) -> GND
- U16 pad 3: +3V3 -> /USB_Hub/USB_DOWN_2/USB1_DN
- U16 pad 4: GND -> /USB_Hub/USB_DOWN_2/USB1_CONN_DN
- U16 pad 5: /MCU/RST -> VBUS
- U16 pad 6: /MCU/UART_TX -> /USB_Hub/USB_DOWN_2/USB1_CONN_DP
- U17 pad 1: VBUS -> /USB_Hub/USB_DOWN_2/USB2_DP
- U17 pad 3: VBUS -> /USB_Hub/USB_DOWN_2/USB2_DN
- U17 pad 4: unconnected-(U17-NC-Pad4) -> /USB_Hub/USB_DOWN_2/USB2_CONN_DN
- U17 pad 5: +3V3 -> VBUS
- U2 pad 1: /USB_Host_Select/USB_A_DP -> /HDMI_Switch/HDMI_IN_A/D0_P
- U2 pad 10: +3V3 -> /HDMI_Switch/HDMI_IN_A/D0_P
- U2 pad 2: /USB_Host_Select/USB_A_DN -> /HDMI_Switch/HDMI_IN_A/D0_N
- U2 pad 3: /USB_Host_Select/USB_B_DP -> GND
- U2 pad 4: /USB_Host_Select/USB_B_DN -> /HDMI_Switch/HDMI_IN_A/CK_P
- U2 pad 5: GND -> /HDMI_Switch/HDMI_IN_A/CK_N
- U2 pad 6: Net-(U2-~{OE}) -> /HDMI_Switch/HDMI_IN_A/CK_N
- U2 pad 7: /UBS_Hub/USB_UP_DN -> /HDMI_Switch/HDMI_IN_A/CK_P
- U2 pad 8: /UBS_Hub/USB_UP_DP -> GND
- U2 pad 9: /SW -> /HDMI_Switch/HDMI_IN_A/D0_N
- U3 pad 1: /USB_Host_Select/USB_CONN_B_DN -> /HDMI_Switch/HDMI_IN_B/D2_P
- U3 pad 2: GND -> /HDMI_Switch/HDMI_IN_B/D2_N
- U3 pad 3: /USB_Host_Select/USB_CONN_B_DP -> GND
- U3 pad 4: /USB_Host_Select/USB_B_DP -> /HDMI_Switch/HDMI_IN_B/D1_P
- U3 pad 5: Net-(U3-VBUS) -> /HDMI_Switch/HDMI_IN_B/D1_N
- U3 pad 6: /USB_Host_Select/USB_B_DN -> /HDMI_Switch/HDMI_IN_B/D1_N
- U4 pad 1: /UBS_Hub/USB_DOWN_1/USB1_DP -> /HDMI_Switch/HDMI_IN_B/D0_P
- U4 pad 10: +3V3 -> /HDMI_Switch/HDMI_IN_B/D0_P
- U4 pad 2: /UBS_Hub/USB_DOWN_1/USB1_DN -> /HDMI_Switch/HDMI_IN_B/D0_N
- U4 pad 3: /UBS_Hub/USB_DOWN_1/USB2_DN -> GND
- U4 pad 4: /UBS_Hub/USB_DOWN_1/USB2_DP -> /HDMI_Switch/HDMI_IN_B/CK_P
- U4 pad 5: +3V3 -> /HDMI_Switch/HDMI_IN_B/CK_N
- U4 pad 6: /UBS_Hub/USB_DOWN_2/USB1_DP -> /HDMI_Switch/HDMI_IN_B/CK_N
- U4 pad 7: /UBS_Hub/USB_DOWN_2/USB1_DN -> /HDMI_Switch/HDMI_IN_B/CK_P
- U4 pad 8: /UBS_Hub/USB_DOWN_2/USB2_DN -> GND
- U4 pad 9: /UBS_Hub/USB_DOWN_2/USB2_DP -> /HDMI_Switch/HDMI_IN_B/D0_N
- U5 pad 1: /UBS_Hub/USB_DOWN_1/USB1_DP -> Net-(U5-AUX_SEL)
- U5 pad 2: GND -> /HDMI_Switch/HDMI_OUT/D2_P
- U5 pad 3: /UBS_Hub/USB_DOWN_1/USB1_DN -> /HDMI_Switch/HDMI_OUT/D2_N
- U5 pad 4: /UBS_Hub/USB_DOWN_1/USB1_CONN_DN -> GND
- U5 pad 5: VBUS -> /HDMI_Switch/HDMI_OUT/D1_P
- U5 pad 6: /UBS_Hub/USB_DOWN_1/USB1_CONN_DP -> /HDMI_Switch/HDMI_OUT/D1_N
- U6 pad 1: /UBS_Hub/USB_DOWN_1/USB2_DP -> /HDMI_Switch/HDMI_OUT/D2_P
- U6 pad 2: GND -> /HDMI_Switch/HDMI_OUT/D2_N
- U6 pad 3: /UBS_Hub/USB_DOWN_1/USB2_DN -> GND
- U6 pad 4: /UBS_Hub/USB_DOWN_1/USB2_CONN_DN -> /HDMI_Switch/HDMI_OUT/D1_P
- U6 pad 5: VBUS -> /HDMI_Switch/HDMI_OUT/D1_N
- U6 pad 6: /UBS_Hub/USB_DOWN_1/USB2_CONN_DP -> /HDMI_Switch/HDMI_OUT/D1_N
- U7 pad 1: /UBS_Hub/USB_DOWN_2/USB1_DP -> /HDMI_Switch/HDMI_OUT/D0_P
- U7 pad 2: GND -> /HDMI_Switch/HDMI_OUT/D0_N
- U7 pad 3: /UBS_Hub/USB_DOWN_2/USB1_DN -> GND
- U7 pad 4: /UBS_Hub/USB_DOWN_2/USB1_CONN_DN -> /HDMI_Switch/HDMI_OUT/CK_P
- U7 pad 5: VBUS -> /HDMI_Switch/HDMI_OUT/CK_N
- U7 pad 6: /UBS_Hub/USB_DOWN_2/USB1_CONN_DP -> /HDMI_Switch/HDMI_OUT/CK_N
- U8 pad 1: /UBS_Hub/USB_DOWN_2/USB2_DP -> VBUS
- U8 pad 3: /UBS_Hub/USB_DOWN_2/USB2_DN -> VBUS
- U8 pad 4: /UBS_Hub/USB_DOWN_2/USB2_CONN_DN -> unconnected-(U8-NC-Pad4)
- U8 pad 5: VBUS -> +3V3
- U9 pad 1: /HDMI_Switch/HDMI_IN_A/D2_P -> unconnected-(U9-PC14-Pad1)
- U9 pad 10: /HDMI_Switch/HDMI_IN_A/D2_P -> /MCU/UP_DET
- U9 pad 2: /HDMI_Switch/HDMI_IN_A/D2_N -> unconnected-(U9-PC15-Pad2)
- U9 pad 3: GND -> +3V3
- U9 pad 4: /HDMI_Switch/HDMI_IN_A/D1_P -> GND
- U9 pad 5: /HDMI_Switch/HDMI_IN_A/D1_N -> /MCU/RST
- U9 pad 6: /HDMI_Switch/HDMI_IN_A/D1_N -> /MCU/UART_TX
- U9 pad 7: /HDMI_Switch/HDMI_IN_A/D1_P -> /MCU/UART_RX
- U9 pad 8: GND -> /MCU/USB_SW
- U9 pad 9: /HDMI_Switch/HDMI_IN_A/D2_N -> /HDMI_Switch/SW
- X1 pad 1: /UBS_Hub/HUB_OSCIN -> /USB_Hub/HUB_OSCIN
- X1 pad 3: /UBS_Hub/HUB_OSCLO -> /USB_Hub/HUB_OSCLO
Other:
- board size 3.6 x 3.2 mm -> 100 x 70 mm
